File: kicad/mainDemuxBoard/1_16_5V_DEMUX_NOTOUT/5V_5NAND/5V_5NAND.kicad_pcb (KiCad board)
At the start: 4 copper layers, 10 parts, among them Q1093 PMOS, Q1094 PMOS, Q1095 PMOS, Q1096 PMOS, Q1097 PMOS, Q1098 NMOS, Q1099 NMOS, Q1100 NMOS, Q1101 NMOS, Q1102 NMOS

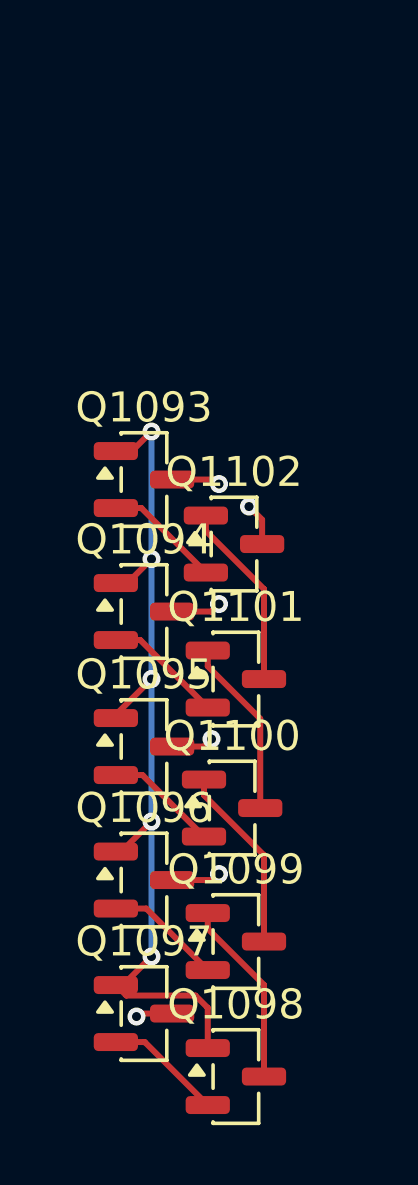
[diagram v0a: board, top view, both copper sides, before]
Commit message: update main board schematic
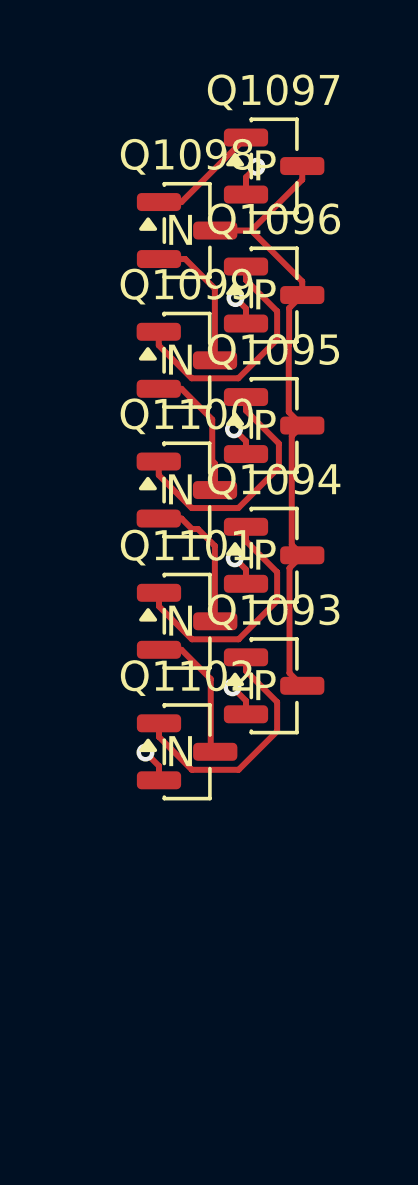
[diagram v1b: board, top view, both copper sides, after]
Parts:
- Q1093, Q1094, Q1095, Q1096, Q1097: value PMOS -> Q_PMOS_GSD; footprint Package_TO_SOT_SMD:SOT-23 -> easyeda2kicad:SOT-23-P
- Q1098, Q1099, Q1100, Q1101, Q1102: value NMOS -> Q_NMOS_GSD; footprint Package_TO_SOT_SMD:SOT-23 -> easyeda2kicad:SOT-23-N
- moved Q1097 28.6 mm to (123.4, 59.9)
- moved Q1098 28.2 mm to (120.5, 62.0)
- moved Q1096 20.0 mm to (123.4, 64.2)
- moved Q1099 19.4 mm to (120.5, 66.4)
- moved Q1095 11.6 mm to (123.4, 68.5)
- moved Q1100 10.7 mm to (120.5, 70.7)
- moved Q1093 8.17 mm to (123.4, 77.2)
- moved Q1102 7.08 mm to (120.5, 79.4)
- moved Q1094 4.79 mm to (123.4, 72.9)
- moved Q1101 2.47 mm to (120.5, 75.1)
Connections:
- Q1093 pad 1: /Y -> /A_{4}
- Q1093 pad 2: /A_{4} -> +5V
- Q1093 pad 3: +5V -> /Y
- Q1094 pad 1: /Y -> /A_{3}
- Q1094 pad 2: /A_{3} -> +5V
- Q1094 pad 3: +5V -> /Y
- Q1095 pad 1: /Y -> /A_{2}
- Q1095 pad 2: /A_{2} -> +5V
- Q1095 pad 3: +5V -> /Y
- Q1096 pad 1: /Y -> /A_{1}
- Q1096 pad 2: /A_{1} -> +5V
- Q1096 pad 3: +5V -> /Y
- Q1097 pad 1: /Y -> /A_{0}
- Q1097 pad 2: /A_{0} -> +5V
- Q1097 pad 3: +5V -> /Y
- Q1098 pad 1: /Y -> /A_{0}
- Q1098 pad 2: /A_{0} -> Net-(Q1098-S)
- Q1098 pad 3: Net-(Q1098-S) -> /Y
- Q1099 pad 1: Net-(Q1098-S) -> /A_{1}
- Q1099 pad 2: /A_{1} -> Net-(Q1099-S)
- Q1099 pad 3: Net-(Q1099-S) -> Net-(Q1098-S)
- Q1100 pad 1: Net-(Q1099-S) -> /A_{2}
- Q1100 pad 2: /A_{2} -> Net-(Q1100-S)
- Q1100 pad 3: Net-(Q1100-S) -> Net-(Q1099-S)
- Q1101 pad 1: Net-(Q1100-S) -> /A_{3}
- Q1101 pad 2: /A_{3} -> Net-(Q1101-S)
- Q1101 pad 3: Net-(Q1101-S) -> Net-(Q1100-S)
- Q1102 pad 1: Net-(Q1101-S) -> /A_{4}
- Q1102 pad 2: /A_{4} -> GND
- Q1102 pad 3: GND -> Net-(Q1101-S)
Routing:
- net /Y: track 30.2 -> 20.9 mm, vias 5 -> 0
- net /A_{2}: track 3.79 -> 8.27 mm
- net /A_{4}: track 3.89 -> 8.27 mm
- net /A_{1}: track 3.91 -> 8.25 mm
- net /A_{3}: track 3.99 -> 8.27 mm
- net +5V: track 7.58 -> 5.15 mm
- net Net-(Q1101-S): track 6.25 -> 4.62 mm
- net Net-(Q1099-S): track 6.23 -> 4.60 mm
- net Net-(Q1098-S): track 6.23 -> 4.66 mm
- net Net-(Q1100-S): track 5.97 -> 4.77 mm
